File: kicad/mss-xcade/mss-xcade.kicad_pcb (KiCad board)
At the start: 2 copper layers, 133.4 x 127 mm, 232 parts, among them J1 Screw_Terminal_01x02, J10 8P8C, J11 Molex 0532610471, J12 Molex 0532610471, J13 Molex 0532610471, J14 Molex 0532610471, J15 Screw_Terminal_01x02, J16 Screw_Terminal_01x02, J17 Screw_Terminal_01x02, J18 Screw_Terminal_01x02, J19 Screw_Terminal_01x02, J2 SM04B-SRSS, J21 Screw_Terminal_01x02, J23 Screw_Terminal_01x02, J24 Screw_Terminal_01x02, J25 Screw_Terminal_01x02, J26 Screw_Terminal_01x02, J27 Molex 0532610471, J28 Molex 0532610471, J29 Molex 0532610471, J3 690-005-299-043, J30 Molex 0532610471, J31 AVR-ISP, J32 SM04B-SRSS, J33 SM04B-SRSS, J34 SM04B-SRSS, J35 SM04B-SRSS, J36 SM04B-SRSS, J37 SM04B-SRSS, J38 SM04B-SRSS, J39 SM04B-SRSS, J4 SM04B-SRSS, J40 SM04B-SRSS, J41 SM04B-SRSS, J42 Screw_Terminal_01x08, J5 Conn_02x03_Odd_Even, J6 SM04B-SRSS, J7 8P8C, J8 8P8C, J9 8P8C, Q1 ZXMS6004FF, Q10 ZXMS6004FF, Q11 ZXMS6004FF, Q12 ZXMS6004FF, Q13 ZXMS6004FF, Q14 ZXMS6004FF, Q15 ZXMS6004FF, Q16 ZXMS6004FF, Q2 ZXMS6004FF, Q3 ZXMS6004FF, Q4 ZXMS6004FF, Q5 ZXMS6004FF, Q6 ZXMS6004FF, Q7 ZXMS6004FF, Q8 ZXMS6004FF, Q9 ZXMS6004FF, SW1 FSM4JSMATR, SW2 SW_DIP_x08, SW3 JS202011SCQN, U1 AZ1117-3.3, U10 74HC4049, U11 TCA9555PWR, U12 ATtiny88-A, U13 TCA9555PWR, U2 AP63205WU, U3 PCA9546ADR, U4 ESP32-S2-SOLO, U5 AP3012, U6 74HC4049, U7 74HC4049, U8 TCA9555PWR, U9 74HC4049

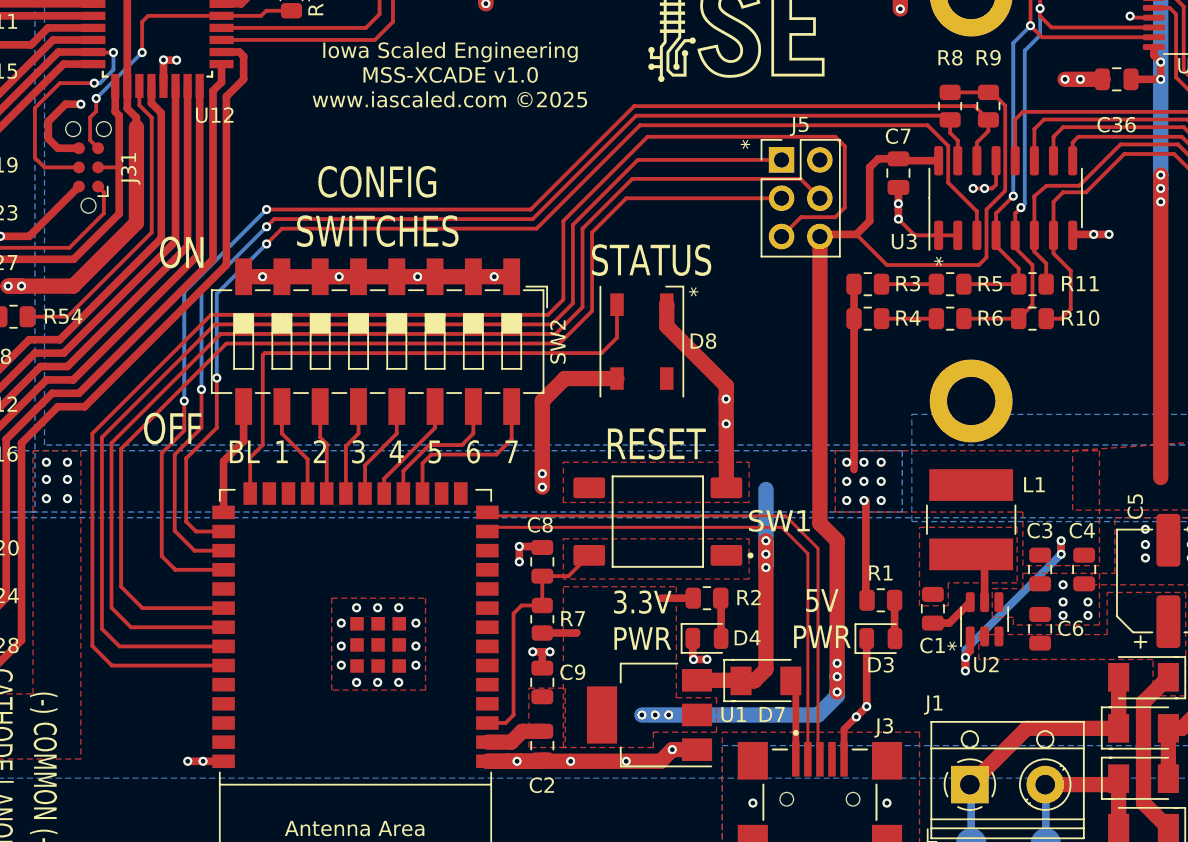
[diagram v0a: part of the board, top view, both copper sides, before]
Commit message: Update expansion connector and add CAN interface module board
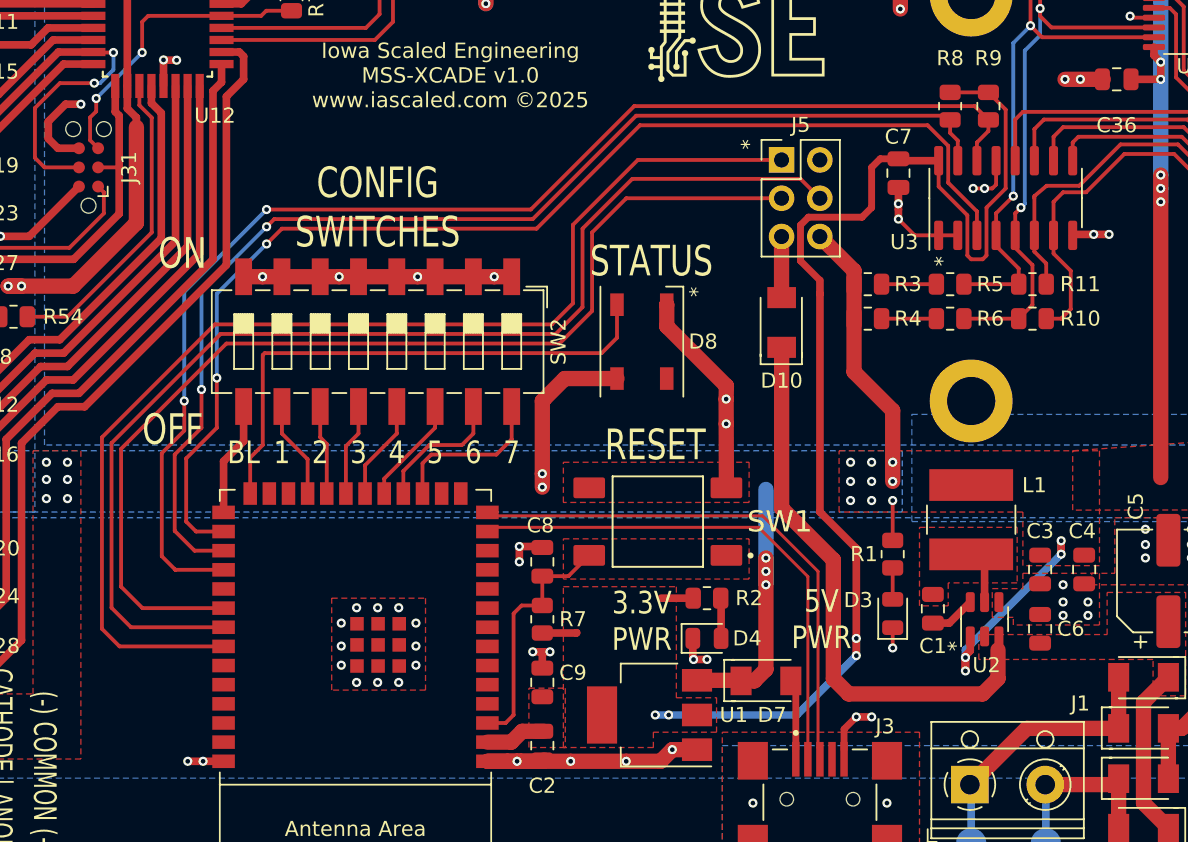
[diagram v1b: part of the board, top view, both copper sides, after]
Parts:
- added D10: CDBM140G, ISE_Generic:SOD-123T, F.Cu at (164.5, 112.6)
- REF1, REF2, REF3: value Fiducial_1mm_Mask2mm -> Fiducial
- moved R1 3.16 mm to (171.8, 128.0), turned to 90 degrees
- moved D3 1.84 mm to (171.8, 132.0), turned to 90 degrees
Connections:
- J5 pad 5: /CAN_AUX2 -> Net-(J5-Pad5)
- J5 pad 6: +3.3V -> +5V
- U4 pad 35: /CAN_AUX2 -> unconnected-(U4-Pad35)
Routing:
- net /CAN_AUX2: track 93.8 -> 0.00 mm
- net /VPWR: track 11.4 -> 48.4 mm
- net Net-(J5-Pad5): track 0.00 -> 4.05 mm
- net +3.3V: track 93.2 -> 90.0 mm, vias 6 -> 4
- net GND: track 368.8 -> 365.7 mm, vias 190 -> 191
- net +5V: track 377.3 -> 379.6 mm
- net /D-: track 35.1 -> 34.2 mm
- net /D+: track 36.3 -> 35.4 mm

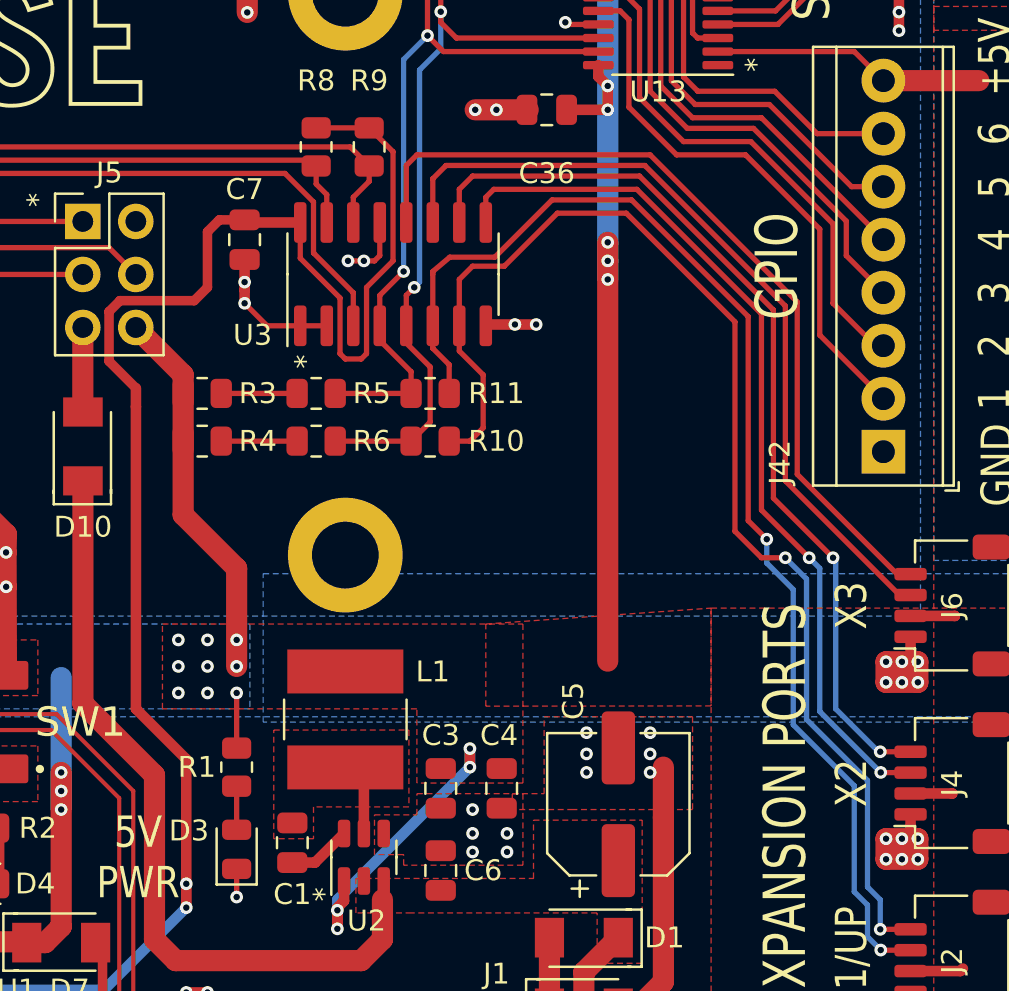
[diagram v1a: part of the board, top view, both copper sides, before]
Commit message: Fix a DRC issue and add some more metal
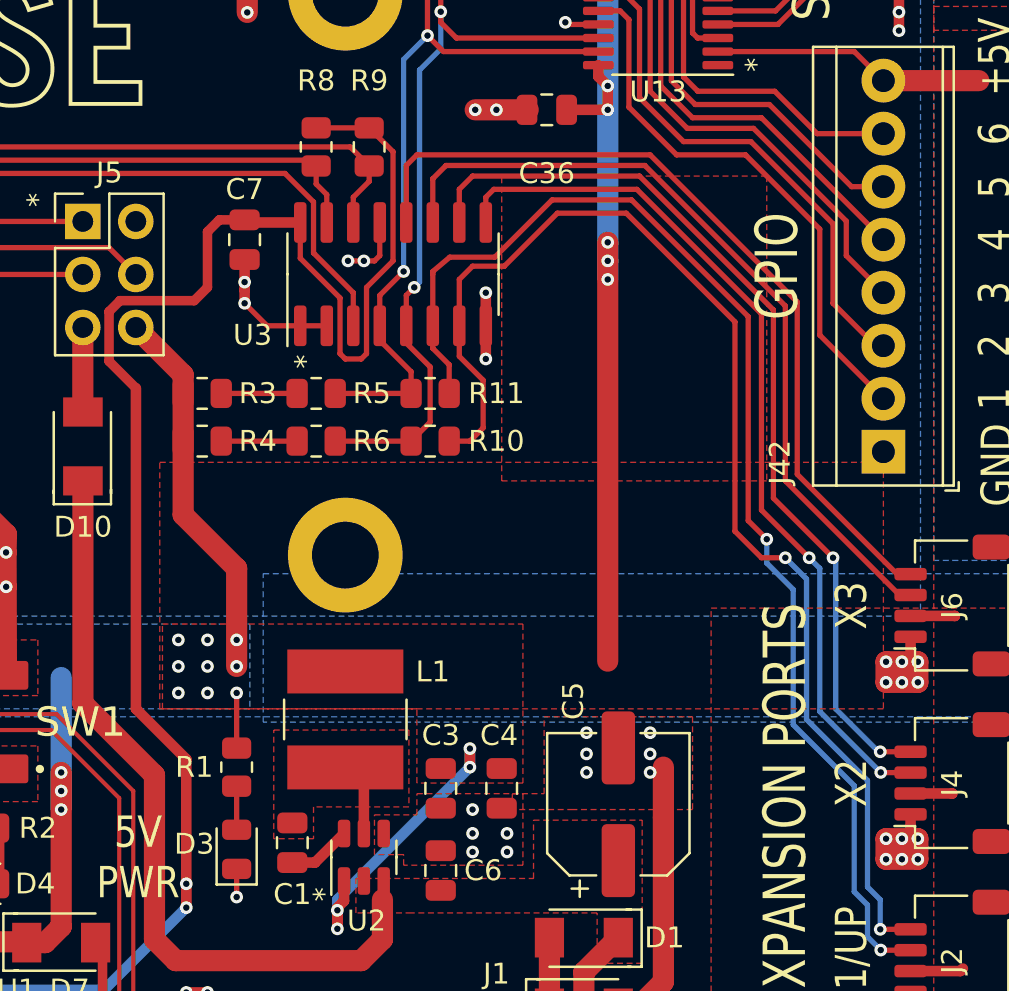
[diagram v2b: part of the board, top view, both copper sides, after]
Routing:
- net GND: track 365.7 -> 366.5 mm
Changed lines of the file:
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@@
   (net 235 "unconnected-(U4-Pad38)")
   (net 236 "unconnected-(U4-Pad39)")
-  (net 237 "Net-(J5-Pad5)")
+  (net 237 "Net-(D10-Pad2)")
   (footprint "Resistor_SMD:R_0805_2012Metric" (layer "F.Cu")
     (at 139.7 55.8165 -90)
@@
       (net 59 "/CAN_RX") (pinfunction "Pin_4") (pintype "passive"))
     (pad "5" thru_hole oval locked (at 0 5.08) (size 1.7 1.7) (drill 1) (layers *.Cu *.Mask)
-      (net 237 "Net-(J5-Pad5)") (pinfunction "Pin_5") (pintype "passive"))
+      (net 237 "Net-(D10-Pad2)") (pinfunction "Pin_5") (pintype "passive"))
     (pad "6" thru_hole oval locked (at 2.54 5.08) (size 1.7 1.7) (drill 1) (layers *.Cu *.Mask)
       (net 3 "+5V") (pinfunction "Pin_6") (pintype "passive"))
@@
     (property "Sheetname" "")
     (attr smd)
-    (fp_text reference "R1" (at 0 -1.905 180) (layer "F.SilkS")
+    (fp_text reference "R1" (at 0 -2.032 180) (layer "F.SilkS")
       (effects (font (size 1 1) (thickness 0.15)))
     )
@@
       (net 1 "/VPWR") (pinfunction "K") (pintype "passive"))
     (pad "2" smd rect (at 1.65 0 90) (size 1.4 1.9) (layers "F.Cu" "F.Paste" "F.Mask")
-      (net 237 "Net-(J5-Pad5)") (pinfunction "A") (pintype "passive"))
+      (net 237 "Net-(D10-Pad2)") (pinfunction "A") (pintype "passive"))
     (model "${KICAD6_3DMODEL_DIR}/Diode_SMD.3dshapes/D_SOD-123.wrl"
       (offset (xyz 0 0 0))
@@
     (property "Sheetname" "")
     (attr smd)
-    (fp_text reference "D3" (at 0.889 -2.286 180) (layer "F.SilkS")
+    (fp_text reference "D3" (at 0.254 -2.032 180) (layer "F.SilkS")
       (effects (font (size 1 1) (thickness 0.15)))
     )
@@
   (segment (start 187.68 92.43) (end 189.1615 92.43) (width 0.254) (layer "F.Cu") (net 2))
   (segment (start 193.294 87.63) (end 193.694 87.23) (width 0.508) (layer "F.Cu") (net 2))
-  (segment (start 183.831 106.807) (end 183.769 106.869) (width 0.508) (layer "F.Cu") (net 2))
   (segment (start 170.434 138.811) (end 169.418 138.811) (width 0.508) (layer "F.Cu") (net 2))
   (segment (start 172.212 105.156) (end 172.212 103.566) (width 0.508) (layer "F.Cu") (net 2))
@@
   (segment (start 186.497 63.82) (end 186.4995 63.8175) (width 0.508) (layer "F.Cu") (net 2))
   (segment (start 197.231 62.611) (end 197.231 63.119) (width 0.508) (layer "F.Cu") (net 2))
+  (segment (start 183.769 108.458) (end 183.769 105.283) (width 0.508) (layer "F.Cu") (net 2))
   (segment (start 186.436 53.467) (end 186.751 53.152) (width 0.508) (layer "F.Cu") (net 2))
   (segment (start 180.975 69.215) (end 180.2765 68.5165) (width 0.254) (layer "F.Cu") (net 2))
@@
   (segment (start 176.149 106.869) (end 173.29 106.869) (width 0.254) (layer "F.Cu") (net 2))
   (segment (start 108.688 32.107) (end 108.688 28.289) (width 0.508) (layer "F.Cu") (net 2))
-  (segment (start 186.182 106.807) (end 183.831 106.807) (width 0.508) (layer "F.Cu") (net 2))
   (segment (start 135.128 53.4035) (end 135.443 53.0885) (width 0.508) (layer "F.Cu") (net 2))
   (segment (start 118.237 35.56) (end 116.459 35.56) (width 0.508) (layer "F.Cu") (net 2))
@@
   (via (at 204.47 139.986) (size 0.6096) (drill 0.3048) (layers "F.Cu" "B.Cu") (net 2))
   (via (at 203.708 139.986) (size 0.6096) (drill 0.3048) (layers "F.Cu" "B.Cu") (net 2))
-  (via (at 185.166 106.807) (size 0.6096) (drill 0.3048) (layers "F.Cu" "B.Cu") (free) (net 2))
+  (via (at 183.769 105.283) (size 0.6096) (drill 0.3048) (layers "F.Cu" "B.Cu") (free) (net 2))
   (via (at 122.663 86.722) (size 0.6096) (drill 0.3048) (layers "F.Cu" "B.Cu") (net 2))
   (via (at 191.643 127.381) (size 0.6096) (drill 0.3048) (layers "F.Cu" "B.Cu") (free) (net 2))
@@
   (via (at 160.78731 119.37469) (size 0.6096) (drill 0.3048) (layers "F.Cu" "B.Cu") (net 2))
   (via (at 203.835 64.897) (size 0.6096) (drill 0.3048) (layers "F.Cu" "B.Cu") (free) (net 2))
-  (via (at 186.182 106.807) (size 0.6096) (drill 0.3048) (layers "F.Cu" "B.Cu") (free) (net 2))
+  (via (at 183.769 108.458) (size 0.6096) (drill 0.3048) (layers "F.Cu" "B.Cu") (free) (net 2))
   (via (at 197.231 63.119) (size 0.6096) (drill 0.3048) (layers "F.Cu" "B.Cu") (net 2))
   (via (at 203.708 140.97) (size 0.6096) (drill 0.3048) (layers "F.Cu" "B.Cu") (net 2))
@@
   (segment (start 144.7955 72.6595) (end 144.7955 73.8) (width 0.508) (layer "F.Cu") (net 3))
   (segment (start 161.5285 72.1205) (end 162.0675 72.6595) (width 0.508) (layer "F.Cu") (net 3))
-  (segment (start 167.005 106.954) (end 167 106.949) (width 1.016) (layer "F.Cu") (net 3))
   (segment (start 121.063 90.646) (end 121.539 90.17) (width 0.508) (layer "F.Cu") (net 3))
   (segment (start 124.714 28.3645) (end 124.714 26.2455) (width 0.508) (layer "F.Cu") (net 3))
@@
   (segment (start 107.688 26.17) (end 107.696 26.162) (width 0.508) (layer "F.Cu") (net 3))
   (segment (start 191.516 85.471) (end 196.088 80.899) (width 1.016) (layer "F.Cu") (net 3))
-  (segment (start 169.2675 110.109) (end 169.291 110.1325) (width 0.508) (layer "F.Cu") (net 3))
-  (segment (start 166.878 107.071) (end 167.142 106.807) (width 0.508) (layer "F.Cu") (net 3))
   (segment (start 123.463 88.46) (end 123.463 86.468) (width 0.508) (layer "F.Cu") (net 3))
   (segment (start 176.657 135.763) (end 176.657 134.874) (width 0.508) (layer "F.Cu") (net 3))
@@
   (segment (start 174.498 132.588) (end 175.5855 132.588) (width 0.508) (layer "F.Cu") (net 7))
   (segment (start 175.5855 132.588) (end 176.977 131.1965) (width 0.508) (layer "F.Cu") (net 7))
-  (segment (start 178.1575 97.409) (end 178.181 97.3855) (width 0.254) (layer "F.Cu") (net 8))
   (segment (start 174.879 103.632) (end 176.784 105.537) (width 0.254) (layer "F.Cu") (net 8))
   (segment (start 169.418 127.635) (end 167.005 125.222) (width 0.508) (layer "F.Cu") (net 8))
@@
   (segment (start 171.003 101.793) (end 170.434 102.362) (width 0.4572) (layer "F.Cu") (net 8))
   (segment (start 150.8525 133.2465) (end 150.876 133.223) (width 0.508) (layer "F.Cu") (net 8))
-  (segment (start 167.005 110.744) (end 167.005 109.855) (width 0.508) (layer "F.Cu") (net 8))
   (segment (start 179.324 98.5285) (end 178.181 97.3855) (width 0.254) (layer "F.Cu") (net 8))
   (segment (start 178.054 108.204) (end 178.054 105.029) (width 0.254) (layer "F.Cu") (net 8))
@@
   (segment (start 178.054 105.029) (end 179.324 103.759) (width 0.254) (layer "F.Cu") (net 8))
   (segment (start 165.7164 106.1906) (end 165.7164 108.5664) (width 0.4572) (layer "F.Cu") (net 8))
-  (segment (start 167.005 125.222) (end 167.005 110.744) (width 0.508) (layer "F.Cu") (net 8))
+  (segment (start 167.005 125.222) (end 167.005 109.855) (width 0.508) (layer "F.Cu") (net 8))
   (segment (start 177.038 108.458) (end 177.8 108.458) (width 0.254) (layer "F.Cu") (net 8))
   (segment (start 176.784 108.204) (end 177.038 108.458) (width 0.254) (layer "F.Cu") (net 8))
@@
   (segment (start 175.641 97.3855) (end 178.181 97.3855) (width 0.254) (layer "F.Cu") (net 8))
   (segment (start 166.2444 105.6654) (end 166.243 105.664) (width 0.4572) (layer "F.Cu") (net 8))
-  (segment (start 178.4115 97.3855) (end 178.181 97.3855) (width 0.254) (layer "F.Cu") (net 8))
   (segment (start 146.5345 140.4855) (end 147.254 139.766) (width 1.016) (layer "F.Cu") (net 8))
   (segment (start 170.434 105.029) (end 169.7976 105.6654) (width 0.4572) (layer "F.Cu") (net 8))
@@
   (segment (start 201.422 133.985) (end 201.422 128.905) (width 0.254) (layer "B.Cu") (net 50))
   (segment (start 121.78975 40.767) (end 123.96825 40.767) (width 0.254) (layer "F.Cu") (net 51))
-  (segment (start 182.499 106.869) (end 182.499 108.077) (width 0.254) (layer "F.Cu") (net 52))
+  (segment (start 183.642 111.76) (end 183.007 112.395) (width 0.254) (layer "F.Cu") (net 52))
+  (segment (start 182.499 106.869) (end 182.499 108.331) (width 0.254) (layer "F.Cu") (net 52))
   (segment (start 184.658 104.013) (end 183.134 104.013) (width 0.254) (layer "F.Cu") (net 52))
   (segment (start 195.707 106.68) (end 190.5 101.473) (width 0.254) (layer "F.Cu") (net 52))
@@
   (segment (start 204.121 135.787) (end 202.668 135.787) (width 0.254) (layer "F.Cu") (net 52))
   (segment (start 198.12 117.983) (end 196.977 117.983) (width 0.254) (layer "F.Cu") (net 52))
-  (segment (start 183.007 112.395) (end 182.0145 112.395) (width 0.254) (layer "F.Cu") (net 52))
   (segment (start 187.198 101.473) (end 184.658 104.013) (width 0.254) (layer "F.Cu") (net 52))
   (segment (start 190.5 101.473) (end 187.198 101.473) (width 0.254) (layer "F.Cu") (net 52))
-  (segment (start 182.499 108.077) (end 183.642 109.22) (width 0.254) (layer "F.Cu") (net 52))
-  (segment (start 183.642 109.22) (end 183.642 111.76) (width 0.254) (layer "F.Cu") (net 52))
-  (segment (start 183.642 111.76) (end 183.007 112.395) (width 0.254) (layer "F.Cu") (net 52))
+  (segment (start 183.642 109.474) (end 183.642 111.76) (width 0.254) (layer "F.Cu") (net 52))
+  (segment (start 182.499 108.331) (end 183.642 109.474) (width 0.254) (layer "F.Cu") (net 52))
+  (segment (start 183.007 112.395) (end 182.0145 112.395) (width 0.254) (layer "F.Cu") (net 52))
   (segment (start 195.707 116.713) (end 195.707 106.68) (width 0.254) (layer "F.Cu") (net 52))
   (segment (start 183.134 104.013) (end 182.499 104.648) (width 0.254) (layer "F.Cu") (net 52))
@@
     (polygon
       (pts
-        (xy 194.564 120.396)
-        (xy 194.565653 125.081571)
-        (xy 183.769 125.095)
-        (xy 183.769 121.158)
+        (xy 202.819 113.411)
+        (xy 202.819 125.222)
+        (xy 168.148 125.222)
+        (xy 168.148 113.411)
       )
     )
@@
       )
     )
+  )
+  (zone (net 3) (net_name "+5V") (layer "F.Cu") (hatch edge 0.508)
+    (connect_pads yes (clearance 0.254))
+    (min_thickness 0.254) (filled_areas_thickness no)
+    (fill yes (thermal_gap 0.508) (thermal_bridge_width 0.508))
+    (polygon
+      (pts
+        (xy 197.231 99.695)
+        (xy 197.231 114.3)
+        (xy 184.531 114.3)
+        (xy 184.531 99.695)
+      )
+    )
